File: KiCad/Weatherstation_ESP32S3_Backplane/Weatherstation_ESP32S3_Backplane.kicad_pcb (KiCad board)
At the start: 2 copper layers, 99.9 x 99.9 mm, 73 parts, among them J1 01x02 JST XH, J10 01x04 Molex KK254, J11 01x02 JST XH, J12 01x04 Molex KK254, J13 01x22 Generic socket, J14 01x22 Generic socket, J15 01x04 Generic header, J16 01x02 JST XH, J17 01x04 Molex KK254, J18 01x02 JST XH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

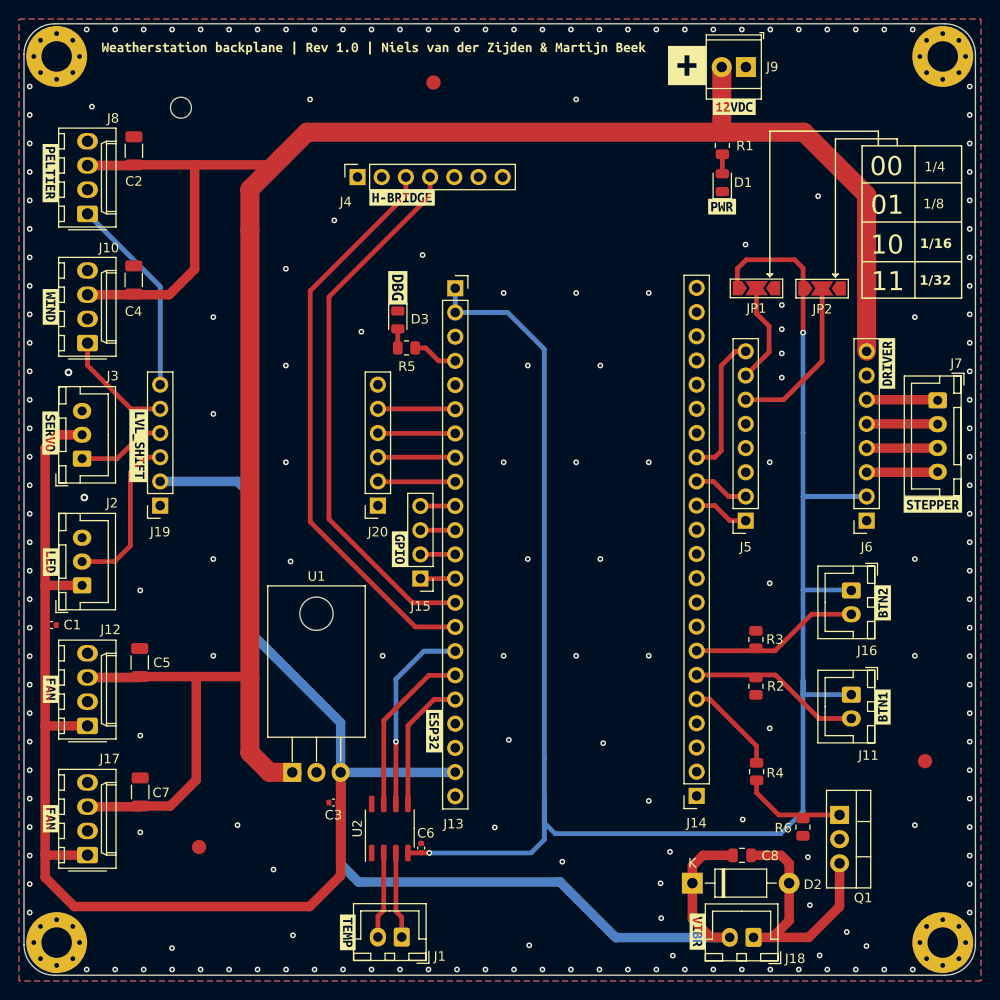
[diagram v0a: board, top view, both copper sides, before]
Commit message: Fixed known issues with PCB: Connected neopixel directly to ESP32, not through level shifter; Exchanged drain & source of vibration motor MOSFET; Added 0,33uF MLCC between pin 1 and gnd of LM7805;
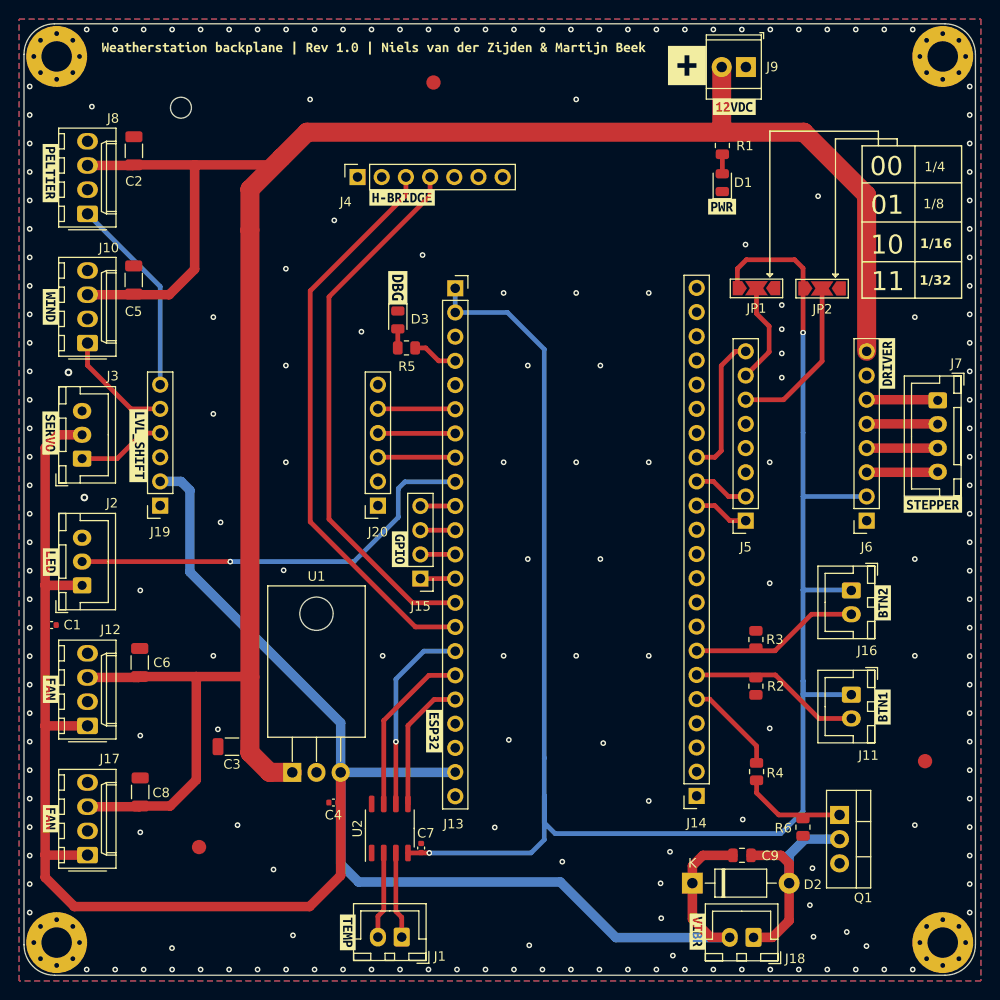
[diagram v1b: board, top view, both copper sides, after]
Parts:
- added C3: 0u33 25V, Capacitor_SMD:C_1206_3216Metric, F.Cu at (154.4, 108.6)
- renumbered C3 to C4, C4 to C5, C5 to C6, C6 to C7, C7 to C8, C8 to C9
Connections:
- J19 pad 3: /LED_DATA_HV -> unconnected-(J19-Pin_3-Pad3)
- J2 pad 2: /LED_DATA_HV -> /LED_DATA
- J20 pad 2: /LED_DATA -> unconnected-(J20-Pin_2-Pad2)
- Q1 pad 2: GND -> Net-(D2-A)
- Q1 pad 3: Net-(D2-A) -> GND
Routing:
- net /LED_DATA: track 8.14 -> 44.4 mm, vias 0 -> 1
- net /LED_DATA_HV: track 17.3 -> 0.00 mm
- net Net-(D2-A): track 27.8 -> 23.8 mm
- net +5V: track 231.0 -> 227.5 mm
- net GND: vias 186 -> 187
